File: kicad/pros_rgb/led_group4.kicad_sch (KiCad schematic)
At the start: 7 parts

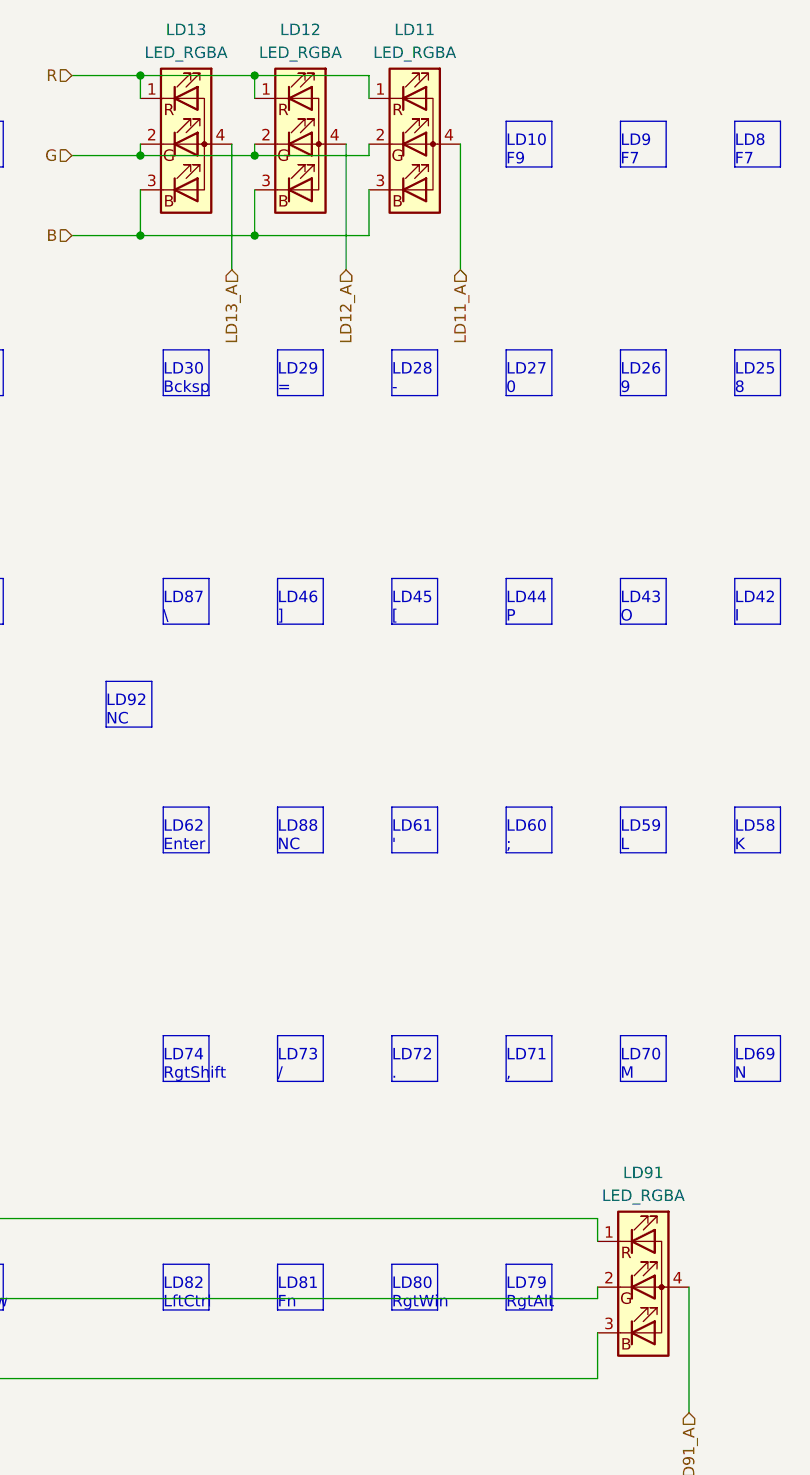
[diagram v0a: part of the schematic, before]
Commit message: kicad/pros_rgb: fix typos
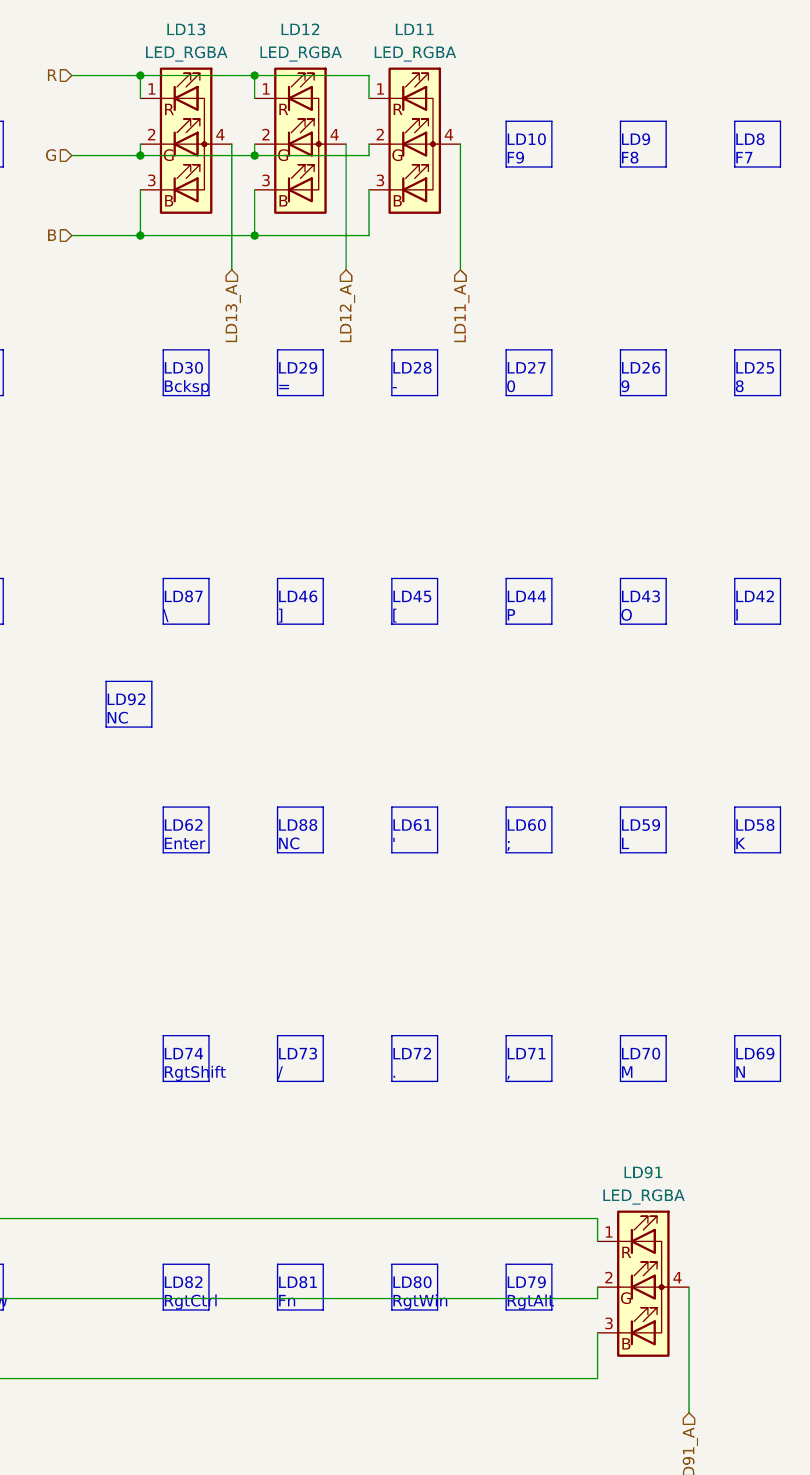
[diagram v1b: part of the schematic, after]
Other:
- note added: "LD82 RgtCtrl"
- note added: "LD9 F8"
- note removed: "LD82 LftCtrl"
- note removed: "LD9 F7"
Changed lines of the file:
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@@
     (effects (font (size 1.27 1.27)) (justify left bottom))
   )
-  (text "LD9\nF7" (at 157.48 29.21 0)
+  (text "LD9\nF8" (at 157.48 29.21 0)
     (effects (font (size 1.27 1.27)) (justify left bottom))
   )
@@
     (effects (font (size 1.27 1.27)) (justify left bottom))
   )
-  (text "LD82\nLftCtrl" (at 106.68 156.21 0)
+  (text "LD82\nRgtCtrl" (at 106.68 156.21 0)
     (effects (font (size 1.27 1.27)) (justify left bottom))
   )

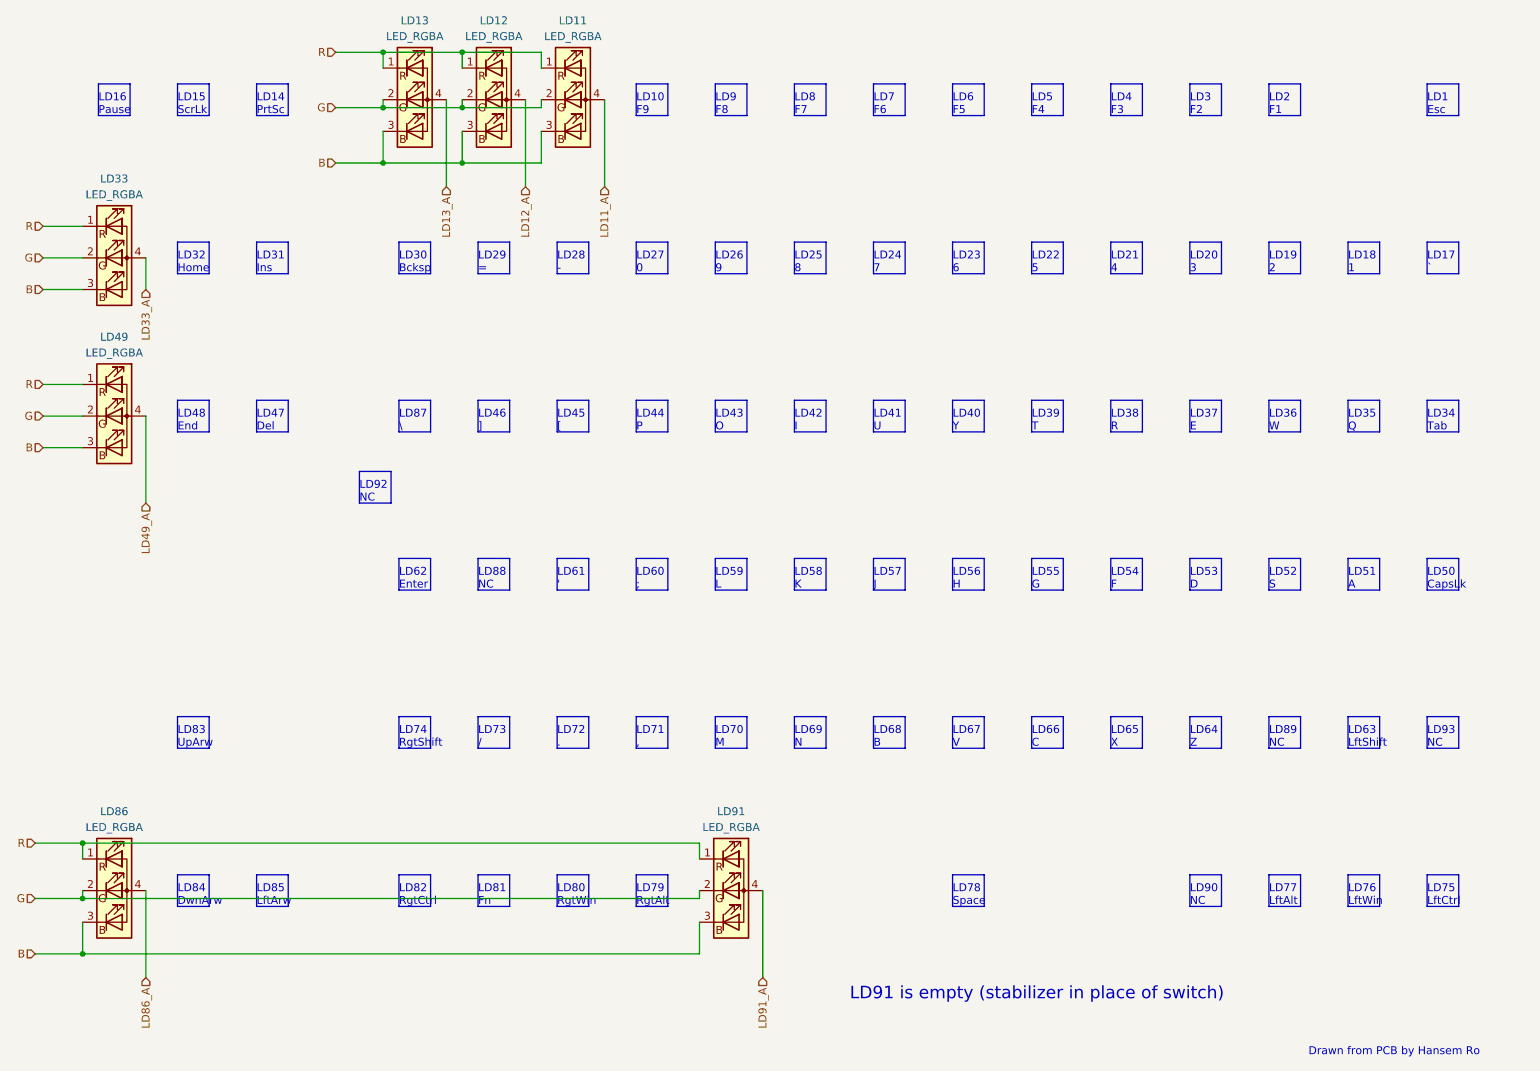
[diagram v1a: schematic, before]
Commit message: kicad/pros_rgb: order led groups by channel number
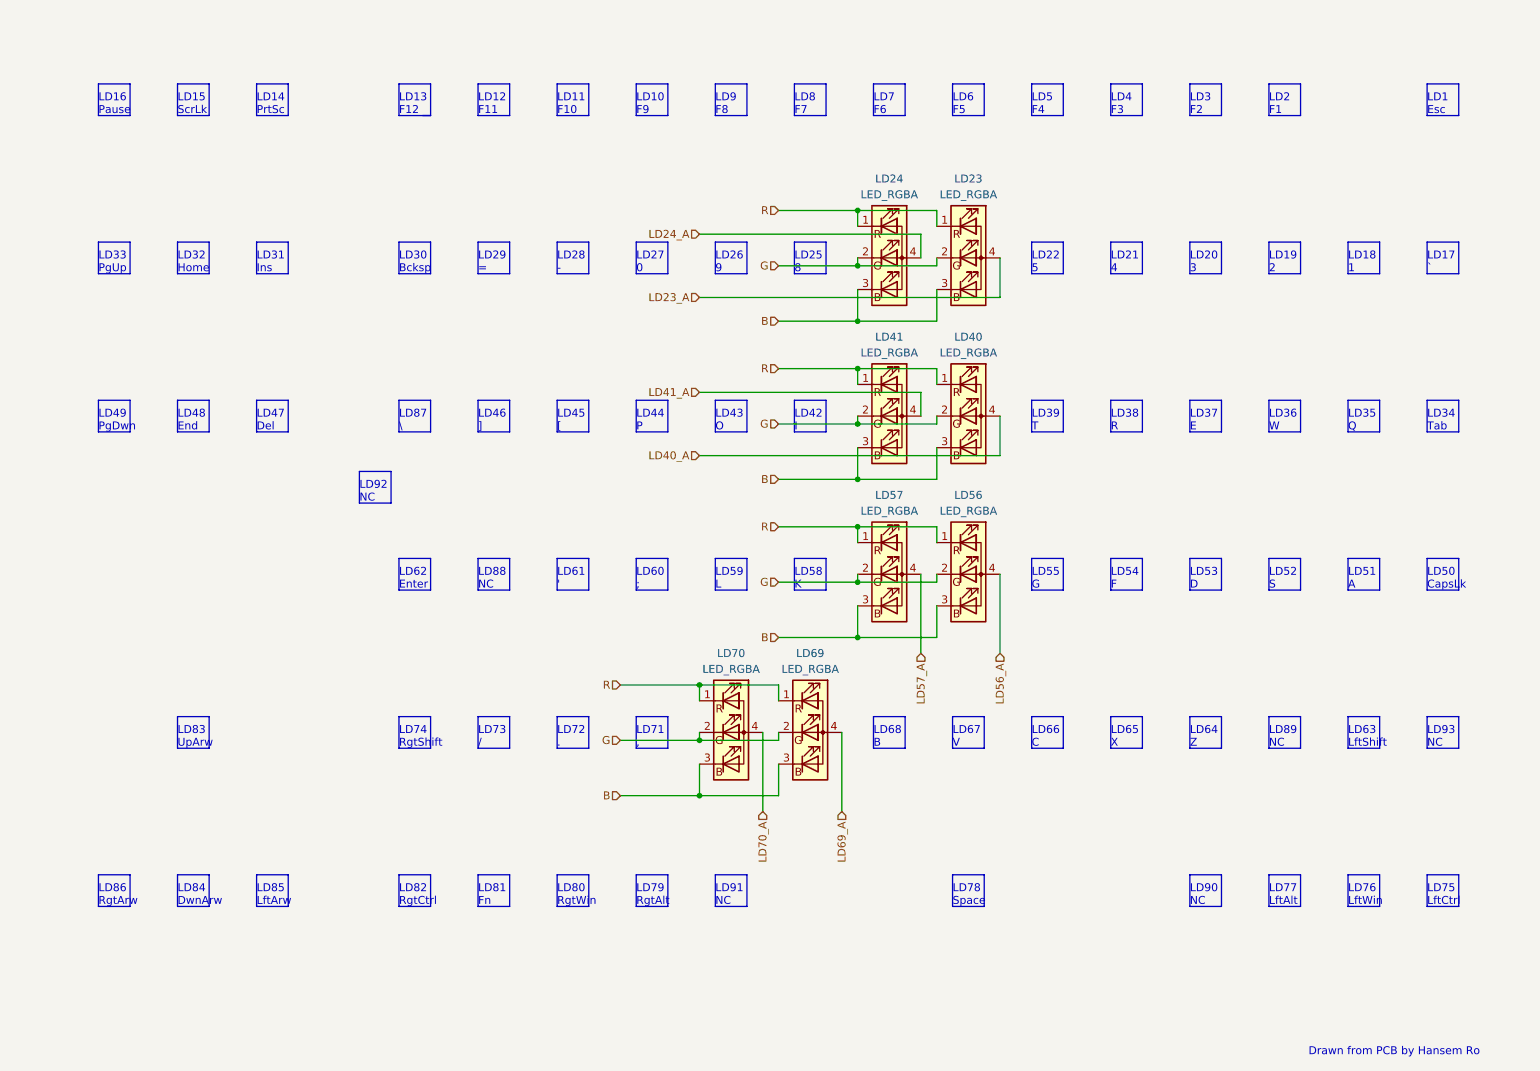
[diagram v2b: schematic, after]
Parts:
- removed LD11, LD12, LD13, LD33, LD49, LD86, LD91: LED_RGBA, symbol Device:LED_RGBA
- added LD23, LD24, LD40, LD41, LD56, LD57, LD69, LD70: LED_RGBA, symbol Device:LED_RGBA
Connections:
- net B: now also LD23.3 (BK), LD24.3 (BK), LD40.3 (BK), LD41.3 (BK), LD56.3 (BK), LD57.3 (BK), LD69.3 (BK), LD70.3 (BK)
- net G: now also LD23.2 (GK), LD24.2 (GK), LD40.2 (GK), LD41.2 (GK), LD56.2 (GK), LD57.2 (GK), LD69.2 (GK), LD70.2 (GK)
- net R: now also LD23.1 (RK), LD24.1 (RK), LD40.1 (RK), LD41.1 (RK), LD56.1 (RK), LD57.1 (RK), LD69.1 (RK), LD70.1 (RK)
- new net LD23_A: LD23.4 (A)
- new net LD24_A: LD24.4 (A)
- new net LD40_A: LD40.4 (A)
- new net LD41_A: LD41.4 (A)
- new net LD56_A: LD56.4 (A)
- new net LD57_A: LD57.4 (A)
- new net LD69_A: LD69.4 (A)
- new net LD70_A: LD70.4 (A)
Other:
- note added: "LD11 F10"
- note added: "LD12 F11"
- note added: "LD13 F12"
- note added: "LD33 PgUp"
- note added: "LD49 PgDwn"
- note added: "LD86 RgtArw"
- note added: "LD91 NC"
- note removed: "LD23 6"
- note removed: "LD24 7"
- note removed: "LD40 Y"
- note removed: "LD41 U"
- note removed: "LD56 H"
- note removed: "LD57 J"
- note removed: "LD69 N"
- note removed: "LD70 M"
- note removed: "LD91 is empty (stabilizer in place of switch)"
